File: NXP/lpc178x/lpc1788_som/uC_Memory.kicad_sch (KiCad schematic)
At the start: 5 parts, among them U1 LPC1788FBD208, U2 LPC1788FBD208, U3 IS42S32160F-7TLI

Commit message: Memory connections
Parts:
- removed U2: LPC1788FBD208, LPC1788FBD208:QFP50P3000X3000X160-208N, symbol _MCU_NXP_LPC:LPC1788FBD208
- added C301, C302, C303, C304, C305, C306, C308, C309, C310, C311, C312, C313: 0u1F, symbol Device:C
- C307: renamed from C1; value C -> 0u1F
- U301: renamed from U4; value ~ -> IS29GL064
- renumbered U1 to U302, U3 to U303
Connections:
- net +3.3V: now also U303.1 (VDD), U303.15 (VDD), U303.29 (VDD), U303.3 (VDDQ), U303.35 (VDDQ), U303.41 (VDDQ), U303.43 (VDD), U303.49 (VDDQ), U303.55 (VDDQ), U303.75 (VDDQ), U303.81 (VDDQ), U303.9 (VDDQ), C301.1, C302.1, C303.1, C304.1, C305.1, C306.1, C308.1, C309.1, C310.1, C311.1, C312.1, C313.1
- net D0: now also U303.2 (DQ0)
- net D1: now also U303.4 (DQ1)
- net D10: now also U303.77 (DQ10)
- net D11: now also U303.79 (DQ11)
- net D12: now also U303.80 (DQ12)
- net D13: now also U303.82 (DQ13)
- net D14: now also U303.83 (DQ14)
- net D15: now also U303.85 (DQ15)
- net D16: now also U303.31 (DQ16)
- net D17: now also U303.33 (DQ17)
- net D18: now also U303.34 (DQ18)
- net D19: now also U303.36 (DQ19)
- net D2: now also U303.5 (DQ2)
- net D20: now also U303.37 (DQ20)
- net D21: now also U303.39 (DQ21)
- net D22: now also U303.40 (DQ22)
- net D23: now also U303.42 (DQ23)
- net D24: now also U303.45 (DQ24)
- net D25: now also U303.47 (DQ25)
- net D26: now also U303.48 (DQ26)
- net D27: now also U303.50 (DQ27)
- net D28: now also U303.51 (DQ28)
- net D29: now also U303.53 (DQ29)
- net D3: now also U303.7 (DQ3)
- net D30: now also U303.54 (DQ30)
- net D31: now also U303.56 (DQ31)
- net D4: now also U303.8 (DQ4)
- net D5: now also U303.10 (DQ5)
- net D6: now also U303.11 (DQ6)
- net D7: now also U303.13 (DQ7)
- net D8: now also U303.74 (DQ8)
- net D9: now also U303.76 (DQ9)
- net GND: now also U303.12 (VSSQ), U303.32 (VSSQ), U303.38 (VSSQ), U303.44 (VSS), U303.46 (VSSQ), U303.52 (VSSQ), U303.58 (VSS), U303.6 (VSSQ), U303.72 (VSS), U303.78 (VSSQ), U303.84 (VSSQ), U303.86 (VSS), C301.2, C302.2, C303.2, C304.2, C305.2, C306.2, C308.2, C309.2, C310.2, C311.2, C312.2, C313.2
- net EMC_DQM0: now reaches U303.16 (DQM0)
- net ~{EMC_WE}: now reaches U303.17 (~{WE})
- net ~{EMC_CAS}: now reaches U303.18 (~{CAS})
- net ~{EMC_RAS}: now reaches U303.19 (~{RAS})
- net ~{EMC_CS}: now reaches U303.20 (~{CS})
- net EMC_DQM2: now reaches U303.28 (DQM2)
- net EMC_DQM3: now reaches U303.59 (DQM3)
- net EMC_CLKE: now reaches U303.67 (CKE)
- net EMC_CLK: now reaches U303.68 (CLK)
- net EMC_DQM1: now reaches U303.71 (DQM1)
- no-connect marks 1 -> 6

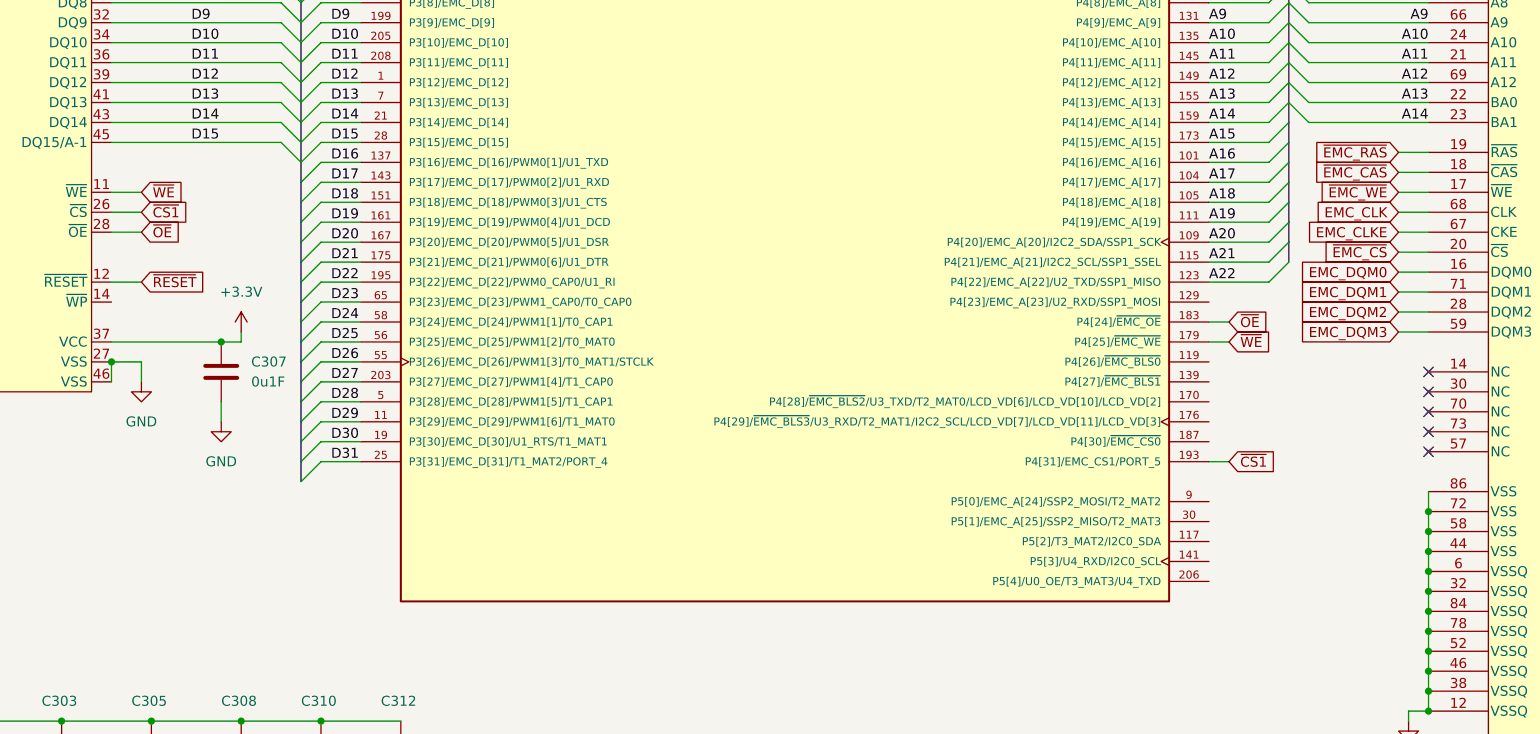
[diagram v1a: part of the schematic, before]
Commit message: Add sodim connector
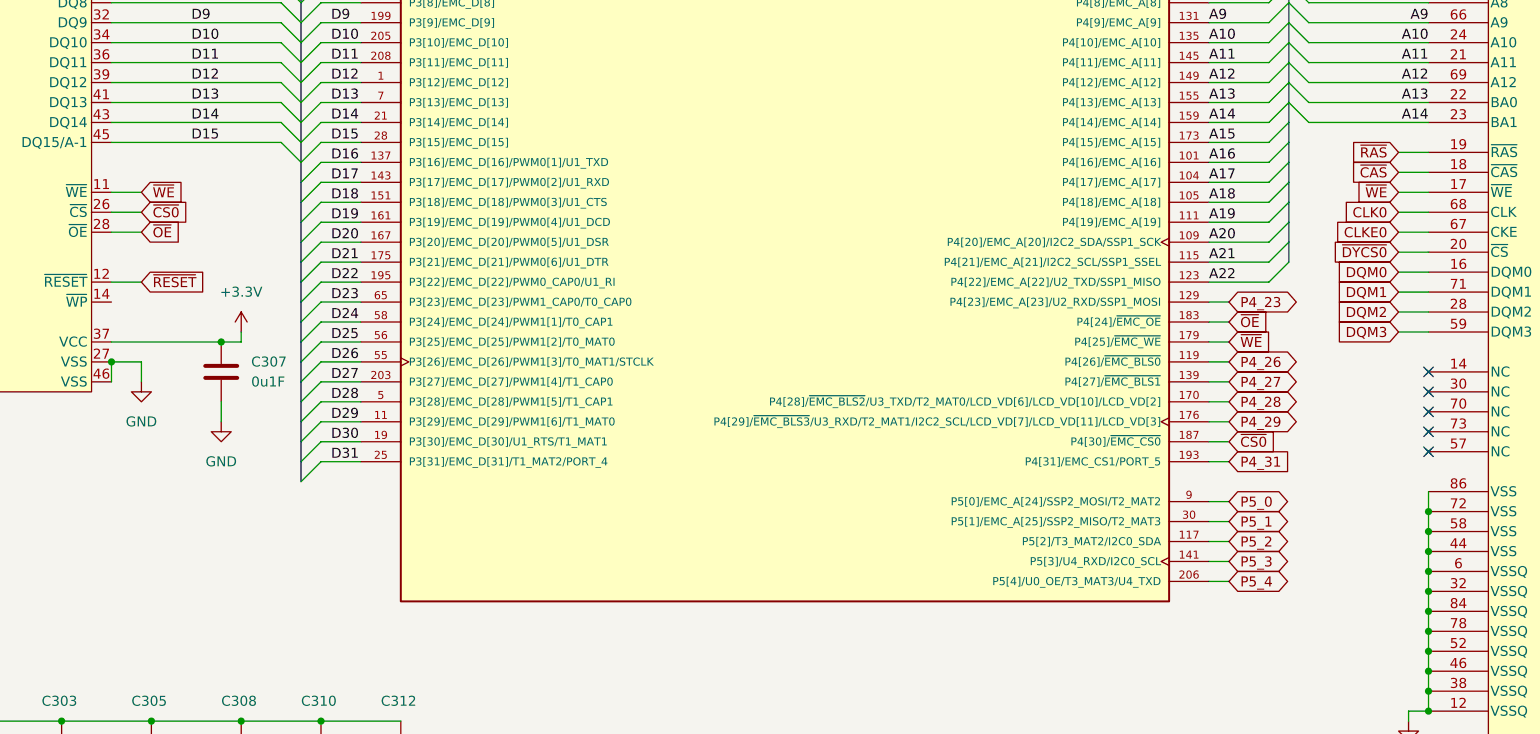
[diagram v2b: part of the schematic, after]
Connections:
- net ~{EMC_WE} is gone; now on net ~{WE}: U303.17 (~{WE})
- net P5_2: now reaches U302.117 (P5[2]/T3_MAT2/I2C0_SDA)
- net P4_26: now reaches U302.119 (P4[26]/~{EMC_BLS0})
- net P4_23: now reaches U302.129 (P4[23]/EMC_A[23]/U2_RXD/SSP1_MOSI)
- net P4_27: now reaches U302.139 (P4[27]/~{EMC_BLS1})
- net P5_3: now reaches U302.141 (P5[3]/U4_RXD/I2C0_SCL)
- net P4_28: now reaches U302.170 (P4[28]/~{EMC_BLS2}/U3_TXD/T2_MAT0/LCD_VD[6]/LCD_VD[10]/LCD_VD[2])
- net P4_29: now reaches U302.176 (P4[29]/~{EMC_BLS3}/U3_RXD/T2_MAT1/I2C2_SCL/LCD_VD[7]/LCD_VD[11]/LCD_VD[3])
- net ~{CS0}: now reaches U302.187 (P4[30]/~{EMC_CS0})
- net ~{CS0}: now also U301.26 (~{CS})
- net P5_4: now reaches U302.206 (P5[4]/U0_OE/T3_MAT3/U4_TXD)
- net P5_1: now reaches U302.30 (P5[1]/EMC_A[25]/SSP2_MISO/T2_MAT3)
- net P5_0: now reaches U302.9 (P5[0]/EMC_A[24]/SSP2_MOSI/T2_MAT2)
- net EMC_CLK renamed CLK0
- net EMC_CLKE renamed CLKE0
- net EMC_DQM0 renamed DQM0
- net EMC_DQM1 renamed DQM1
- net EMC_DQM2 renamed DQM2
- net EMC_DQM3 renamed DQM3
- net ~{CS1} renamed P4_31
- net P4_31: no longer U301.26 (~{CS})
- net ~{EMC_CAS} renamed ~{CAS}
- net ~{EMC_CS} renamed ~{DYCS0}
- net ~{EMC_RAS} renamed ~{RAS}

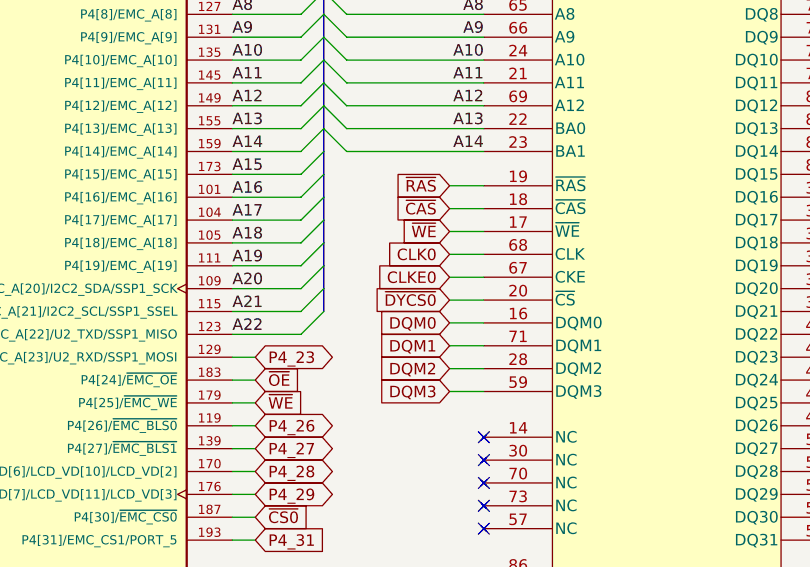
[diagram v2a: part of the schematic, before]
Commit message: LPC1788
Added LPC1788 som module
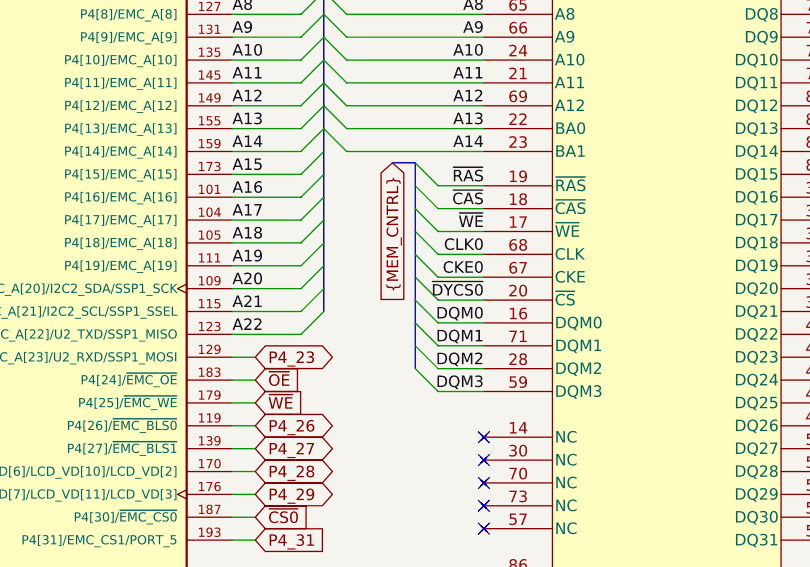
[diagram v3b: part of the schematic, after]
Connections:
- net CLKE0 renamed CKE0
